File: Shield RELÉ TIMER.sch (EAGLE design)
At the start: 44 parts, among them K1 JS-M1-9V-5, K2 JS-M1-9V-5, K3 JS-M1-9V-5, K4 JS-M1-9V-5, K5 JS-M1-9V-5, K6 JS-M1-9V-5, M1 ARDUINO-NANO-3.0, Q1 BC548, Q2 BC548, Q3 BC548, Q4 BC548, Q5 BC548, Q6 BC548

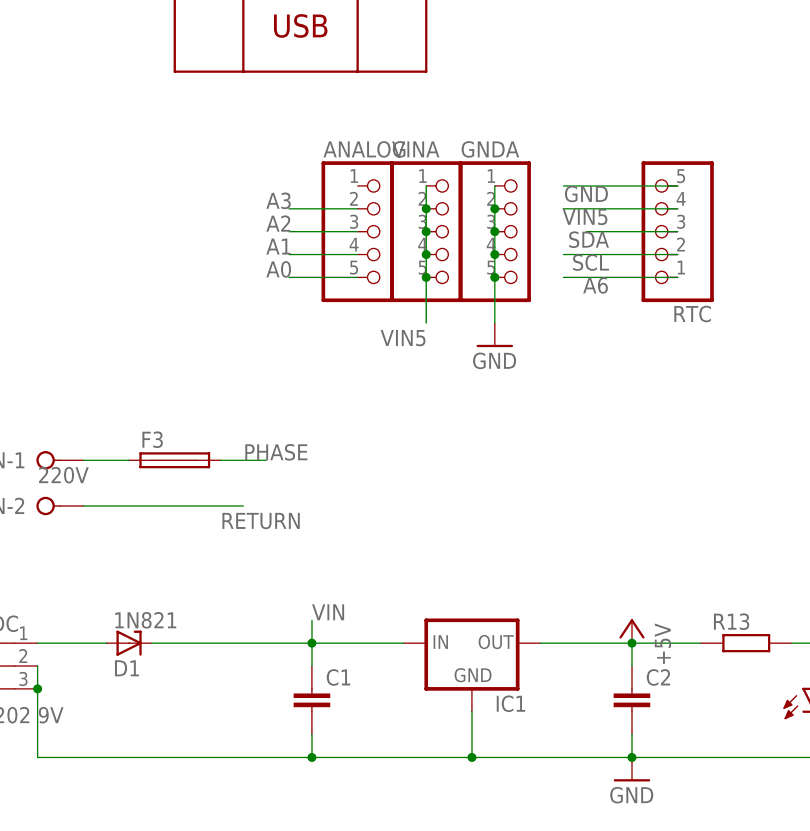
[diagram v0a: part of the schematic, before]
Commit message: Change-size
Redução de tamanho impresso
Mudança nas vias dos transistor para utilização de JUMPERS
Mudança layout do regulador 7805
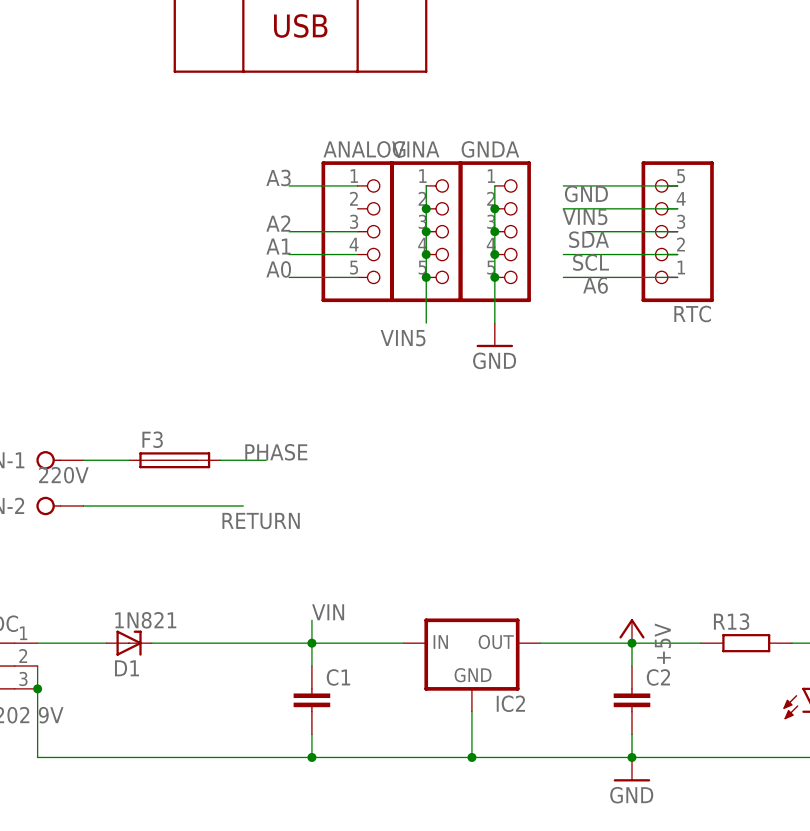
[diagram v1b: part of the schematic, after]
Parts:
- removed IC1: (no value), v-reg:78XXL
- added IC2: (no value), v-reg:78XXS
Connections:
- net +5V: now also IC2.OUT; no longer IC1.OUT
- net A3: now also ANALOG.1; no longer ANALOG.2
- net GND: now also IC2.GND; no longer IC1.GND
- net VIN: now also IC2.IN; no longer IC1.IN
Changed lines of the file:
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@@
 <part name="RELE_6" library="con-wago-508" library_urn="urn:adsk.eagle:library:196" deviceset="W237-03P" device="" package3d_urn="urn:adsk.eagle:package:10737/1"/>
 <part name="VIN_DC" library="con-jack" library_urn="urn:adsk.eagle:library:154" deviceset="DCJ0202" device="" package3d_urn="urn:adsk.eagle:package:7491/1" value="DCJ0202  9V"/>
-<part name="IC1" library="v-reg" library_urn="urn:adsk.eagle:library:409" deviceset="78XXL" device="" package3d_urn="urn:adsk.eagle:package:30361/1"/>
 <part name="C1" library="rcl" library_urn="urn:adsk.eagle:library:334" deviceset="C-EU" device="025-030X050" package3d_urn="urn:adsk.eagle:package:23631/1"/>
 <part name="C2" library="rcl" library_urn="urn:adsk.eagle:library:334" deviceset="C-EU" device="025-030X050" package3d_urn="urn:adsk.eagle:package:23631/1"/>
@@
 <part name="F3" library="fuse" library_urn="urn:adsk.eagle:library:233" deviceset="SH25" device="" package3d_urn="urn:adsk.eagle:package:14066/1"/>
 <part name="D1" library="diode" library_urn="urn:adsk.eagle:library:210" deviceset="1N821" device="" package3d_urn="urn:adsk.eagle:package:43342/1"/>
+<part name="IC2" library="v-reg" library_urn="urn:adsk.eagle:library:409" deviceset="78XXS" device="" package3d_urn="urn:adsk.eagle:package:30342/1"/>
 </parts>
 <sheets>
@@
 <instance part="RELE_6" gate="-3" x="246.38" y="81.28"/>
 <instance part="VIN_DC" gate="G$1" x="43.18" y="86.36"/>
-<instance part="IC1" gate="A" x="99.06" y="88.9"/>
 <instance part="C1" gate="G$1" x="81.28" y="83.82"/>
 <instance part="C2" gate="G$1" x="116.84" y="83.82"/>
@@
 <instance part="F3" gate="1" x="66.04" y="109.22"/>
 <instance part="D1" gate="1" x="60.96" y="88.9" rot="MR180"/>
+<instance part="IC2" gate="1" x="99.06" y="88.9"/>
 </instances>
 <busses>
@@
 </segment>
 <segment>
-<pinref part="IC1" gate="A" pin="OUT"/>
 <pinref part="C2" gate="G$1" pin="1"/>
 <wire x1="106.68" y1="88.9" x2="116.84" y2="88.9" width="0.1524" layer="91"/>
@@
 <pinref part="R13" gate="G$1" pin="1"/>
 <wire x1="116.84" y1="88.9" x2="124.46" y2="88.9" width="0.1524" layer="91"/>
+<pinref part="IC2" gate="1" pin="OUT"/>
 </segment>
 </net>
@@
 <pinref part="C2" gate="G$1" pin="2"/>
 <wire x1="116.84" y1="76.2" x2="116.84" y2="78.74" width="0.1524" layer="91"/>
-<pinref part="IC1" gate="A" pin="GND"/>
 <wire x1="99.06" y1="81.28" x2="99.06" y2="76.2" width="0.1524" layer="91"/>
 <wire x1="99.06" y1="76.2" x2="116.84" y2="76.2" width="0.1524" layer="91"/>
@@
 <pinref part="LED7" gate="G$1" pin="C"/>
 <junction x="137.16" y="78.74"/>
+<pinref part="IC2" gate="1" pin="GND"/>
 </segment>
 <segment>
@@
 </segment>
 <segment>
-<pinref part="ANALOG" gate="A" pin="2"/>
-<wire x1="86.36" y1="137.16" x2="78.74" y2="137.16" width="0.1524" layer="91"/>
-<label x="76.2" y="137.16" size="1.778" layer="95"/>
+<pinref part="ANALOG" gate="A" pin="1"/>
+<wire x1="86.36" y1="139.7" x2="78.74" y2="139.7" width="0.1524" layer="91"/>
+<label x="76.2" y="139.7" size="1.778" layer="95"/>
 </segment>
 </net>
@@
 </segment>
 <segment>
-<pinref part="IC1" gate="A" pin="IN"/>
 <wire x1="63.5" y1="88.9" x2="81.28" y2="88.9" width="0.1524" layer="91"/>
 <pinref part="C1" gate="G$1" pin="1"/>
@@
 <label x="81.28" y="91.44" size="1.778" layer="95"/>
 <pinref part="D1" gate="1" pin="C"/>
-</segment>
-</net>
+<pinref part="IC2" gate="1" pin="IN"/>
+</segment>
+</net>
